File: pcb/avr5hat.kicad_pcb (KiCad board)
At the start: 2 copper layers, 65 x 56 mm, 21 parts, among them J1 GPIO, J2 AVR1, J3 AVR2, J4 AVR3, J5 AVR4, J6 AVR5, J7 Aux, U1 TXS0108EPW, U2 TXS0108EPW, U3 TXS0108EPW

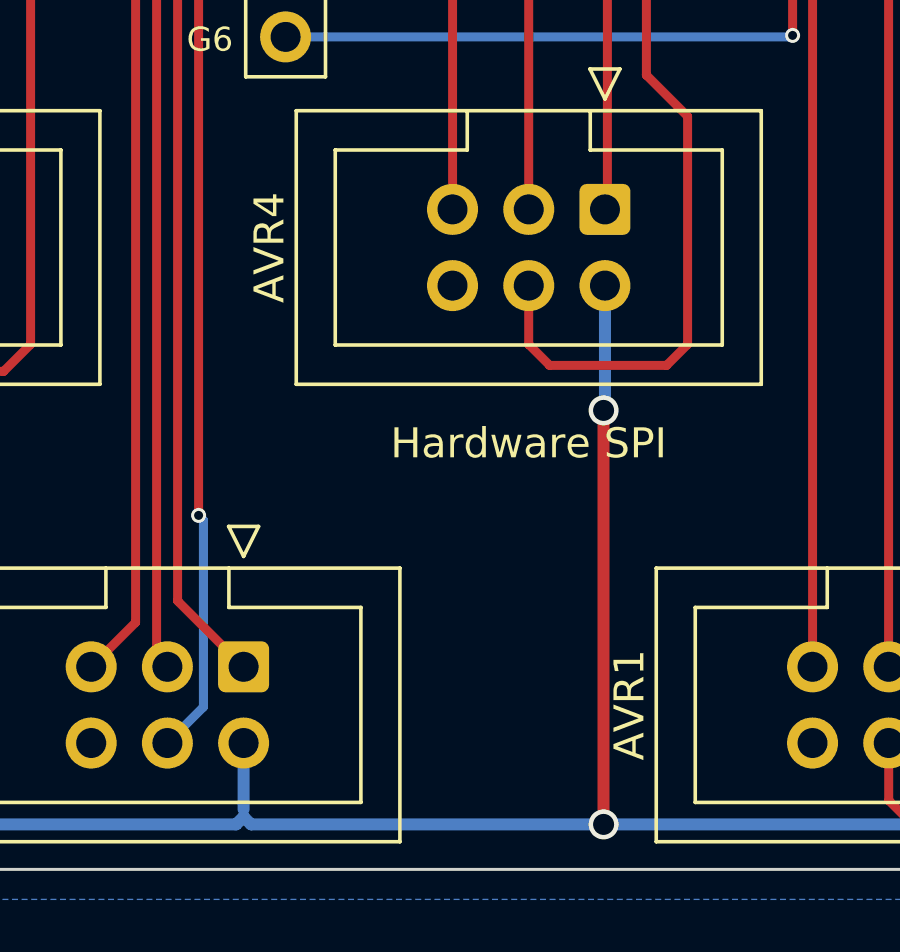
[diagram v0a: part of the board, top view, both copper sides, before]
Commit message: swap refs
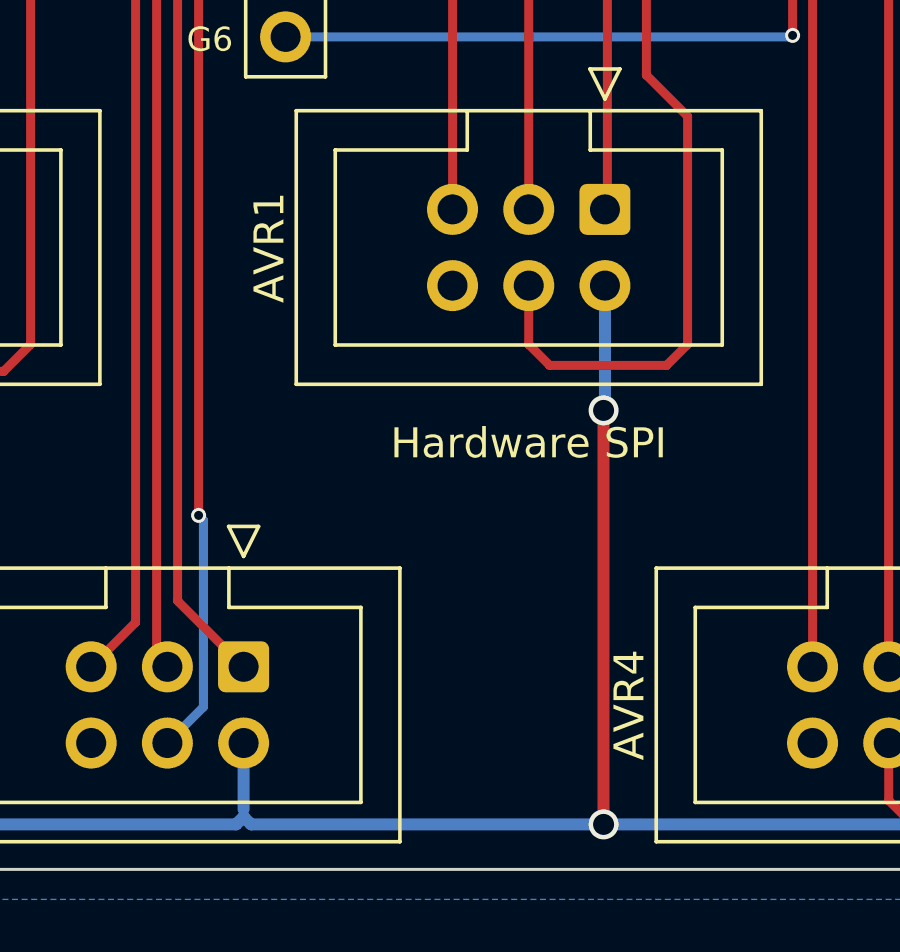
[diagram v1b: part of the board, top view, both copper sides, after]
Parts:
- J2: value AVR1 -> AVR4
- J5: value AVR4 -> AVR1
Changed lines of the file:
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@@
     )
   )
-  (footprint "Symbol:OSHW-Symbol_6.7x6mm_SilkScreen" (layer "F.Cu")
+  (footprint "Symbol:OSHW-Symbol_6.7x6mm_SilkScreen" locked (layer "F.Cu")
     (at 106.25 63.55)
     (descr "Open Source Hardware Symbol")
@@
       (effects (font (size 1 1) (thickness 0.15)))
     )
-    (fp_text value "AVR1" (at 1.27 11.18 -270) (layer "F.SilkS")
+    (fp_text value "AVR4" (at 1.27 11.18 -270) (layer "F.SilkS")
       (effects (font (size 1 1) (thickness 0.15)))
     )
@@
       (effects (font (size 1 1) (thickness 0.15)))
     )
-    (fp_text value "AVR4" (at 1.27 11.18 90) (layer "F.SilkS")
-      (effects (font (size 1 1) (thickness 0.15)))
-    )
+    (fp_text value "AVR1" (at 1.27 11.18 90) (layer "F.SilkS")
+      (effects (font (size 1 1) (thickness 0.15)))
+    )

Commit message: v1
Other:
- board text added: "avr5hat v1 github.com/gcormier/avr5hat"
- board text removed: "avr5hat github.com/gcormier/avr5hat"
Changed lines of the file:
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@@
     (effects (font (size 0.8 0.8) (thickness 0.12)))
   )
-  (gr_text "avr5hat\ngithub.com/gcormier/avr5hat" (at 146.1 67.5) (layer "F.SilkS")
+  (gr_text "avr5hat v1\ngithub.com/gcormier/avr5hat" (at 146.1 67.5) (layer "F.SilkS")
     (effects (font (size 1.5 1.5) (thickness 0.2)))
   )

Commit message: add jlc silkscreen
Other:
- board text added: "JLCJLCJLCJLC"
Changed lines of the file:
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@@
     (property "Sheetname" "")
     (attr smd)
-    (fp_text reference "U1" (at 0 0 -180) (layer "F.SilkS")
+    (fp_text reference "U1" (at 0 0 -180) (layer "F.SilkS") hide
       (effects (font (size 1 1) (thickness 0.15)))
     )
@@
   (gr_line (start 100 81) (end 100 97) (layer "Edge.Cuts") (width 0.1))
   (gr_line (start 162 44) (end 103 44) (layer "Edge.Cuts") (width 0.1))
+  (gr_text "JLCJLCJLCJLC" (at 132.5 87.9) (layer "B.SilkS")
+    (effects (font (size 1 1) (thickness 0.15)) (justify mirror))
+  )
   (gr_text "Hardware SPI" (at 132.5 85.8) (layer "F.SilkS")
     (effects (font (size 1 1) (thickness 0.15)))

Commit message: 3v3 versiony
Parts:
- removed C1, C2, C3, C4, C5, C6: 0.1uF, Capacitor_SMD:C_0603_1608Metric
- removed U1, U2, U3: TXS0108EPW, Package_SO:TSSOP-20_4.4x6.5mm_P0.65mm
- moved J7 4.82 mm to (125.1, 54.8)
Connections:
- J1 pad 2: +5V -> unconnected-(J1-Pad2)
- J1 pad 4: +5V -> unconnected-(J1-Pad4)
- J2 pad 1: MISO5_4 -> MISO_4
- J2 pad 2: +5V -> +3V3
- J2 pad 3: SCK5_4 -> SCK_4
- J2 pad 4: MOSI5_4 -> MOSI_4
- J2 pad 5: RST5_4 -> RST_4
- J3 pad 1: MISO5_2 -> MISO_2
- J3 pad 2: +5V -> +3V3
- J3 pad 3: SCK5_2 -> SCK_2
- J3 pad 4: MOSI5_2 -> MOSI_2
- J3 pad 5: RST5_2 -> RST_2
- J4 pad 1: MISO5_3 -> MISO_3
- J4 pad 2: +5V -> +3V3
- J4 pad 3: SCK5_3 -> SCK_3
- J4 pad 4: MOSI5_3 -> MOSI_3
- J4 pad 5: RST5_3 -> RST_3
- J5 pad 1: MISO5_1 -> MISO_1
- J5 pad 2: +5V -> +3V3
- J5 pad 3: SCK5_1 -> SCK_1
- J5 pad 4: MOSI5_1 -> MOSI_1
- J5 pad 5: RST5_1 -> RST_1
- J6 pad 1: MISO5_5 -> MISO_5
- J6 pad 2: +5V -> +3V3
- J6 pad 3: SCK5_5 -> SCK_5
- J6 pad 4: MOSI5_5 -> MOSI_5
- J6 pad 5: RST5_5 -> RST_5
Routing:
- net +5V: track 249.1 -> 0.00 mm, vias 9 -> 0
- net +3V3: track 76.9 -> 196.3 mm
- net MOSI_4: track 9.44 -> 59.8 mm
- net MOSI5_4: track 44.9 -> 0.00 mm
- net MOSI_3: track 10.6 -> 50.7 mm
- net MISO_3: track 8.50 -> 47.6 mm
- net RST_3: track 11.5 -> 50.5 mm
- net SCK_4: track 10.0 -> 48.9 mm
- net MISO_4: track 6.71 -> 45.3 mm
- net SCK_3: track 11.5 -> 49.7 mm
- net MOSI5_3: track 36.5 -> 0.00 mm, vias 1 -> 0
- net MOSI_5: track 10.1 -> 46.4 mm
- net RST_4: track 9.39 -> 45.3 mm
- net MOSI_1: track 11.3 -> 46.8 mm
- net RST5_4: track 35.1 -> 0.00 mm
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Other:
- board text added: "3.3V Only"
- board text removed: "3V Only"
